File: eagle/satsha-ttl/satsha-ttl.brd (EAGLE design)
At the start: 49 x 31 mm, 17 parts, among them IC1 MCP1703DB, U2 CH340G

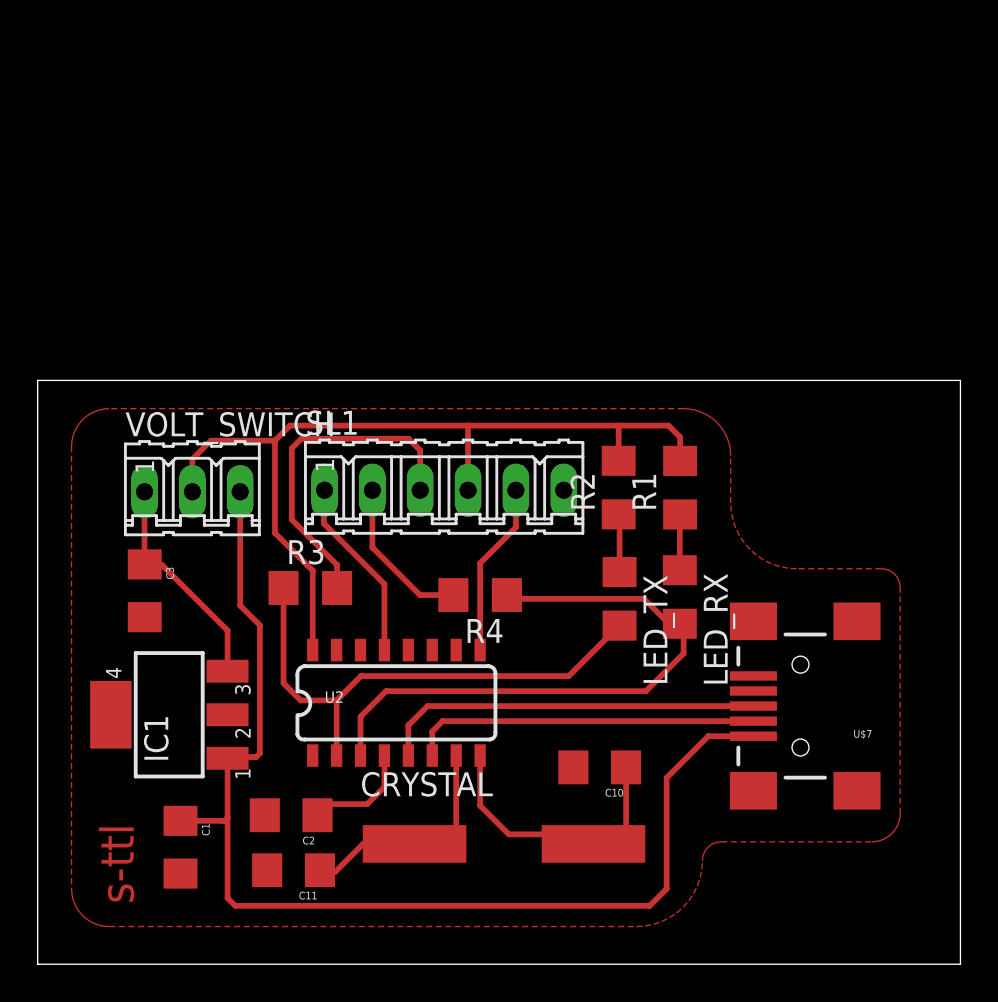
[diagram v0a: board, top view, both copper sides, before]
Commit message: added pngs for 0.2mm
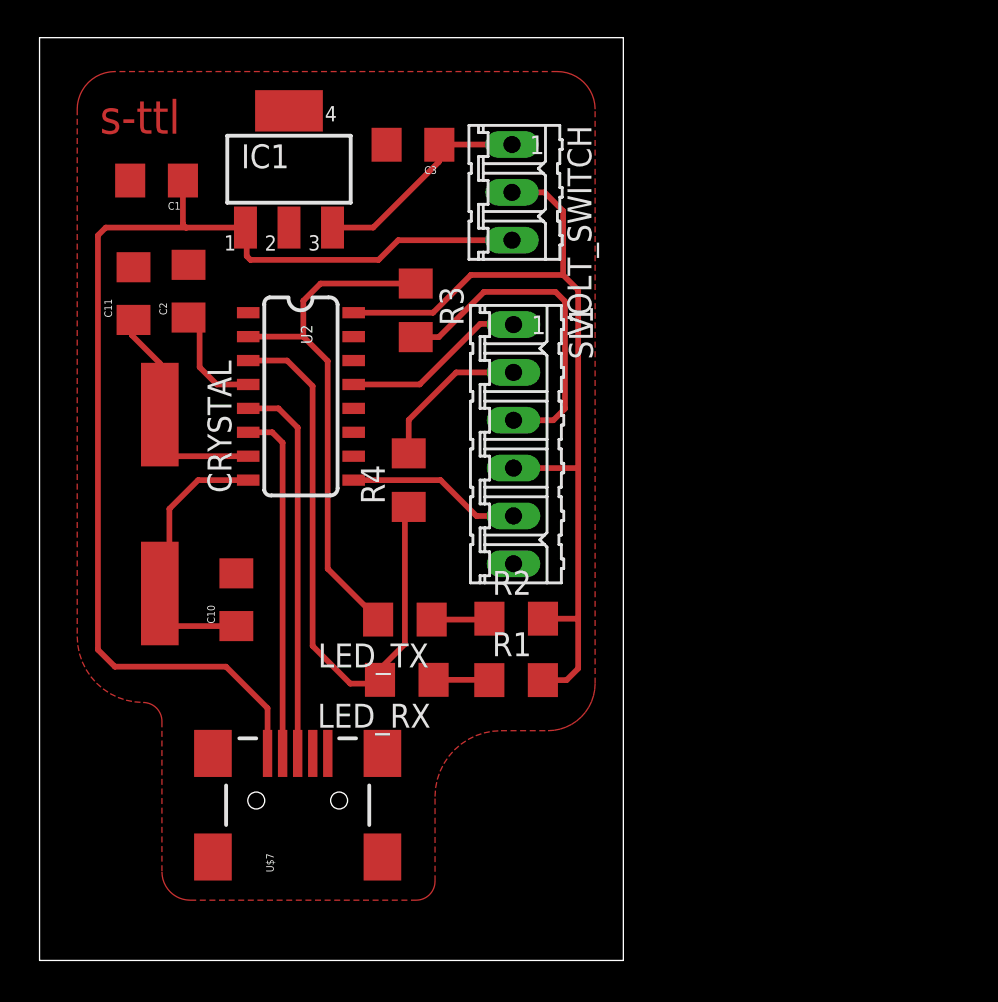
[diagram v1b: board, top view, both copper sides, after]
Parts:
- moved C1 35.4 mm to (6.41, 41.8), turned to 180 degrees
- moved C11 31.8 mm to (5.19, 35.8), turned to 90 degrees
- moved IC1 29.7 mm to (13.4, 42.4), turned to 0 degrees
- moved C2 28.4 mm to (8.11, 35.9), turned to 90 degrees
- moved C3 27.6 mm to (20.0, 43.7), turned to 180 degrees
- moved U$7 27.2 mm to (13.9, 8.89), turned to 90 degrees
- moved CRYSTAL 25.7 mm to (6.59, 24.6), turned to 270 degrees
- moved VOLT_SWITCH 23.3 mm to (25.3, 41.2), turned to 270 degrees
- moved C10 21.2 mm to (10.7, 19.6), turned to 90 degrees
- moved U2 17.0 mm to (14.1, 30.4), turned to 270 degrees
- moved R3 15.8 mm to (20.2, 34.9), turned to 270 degrees
- moved LED_RX 15.2 mm to (19.7, 15.3), turned to 180 degrees
- moved R1 13.4 mm to (25.5, 15.3), turned to 0 degrees
- moved LED_TX 11.5 mm to (19.6, 18.5), turned to 180 degrees
- moved R2 8.84 mm to (25.5, 18.5), turned to 0 degrees
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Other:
- board size 49 x 31 mm -> 31 x 49 mm
